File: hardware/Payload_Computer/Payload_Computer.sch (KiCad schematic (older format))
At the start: 0 parts

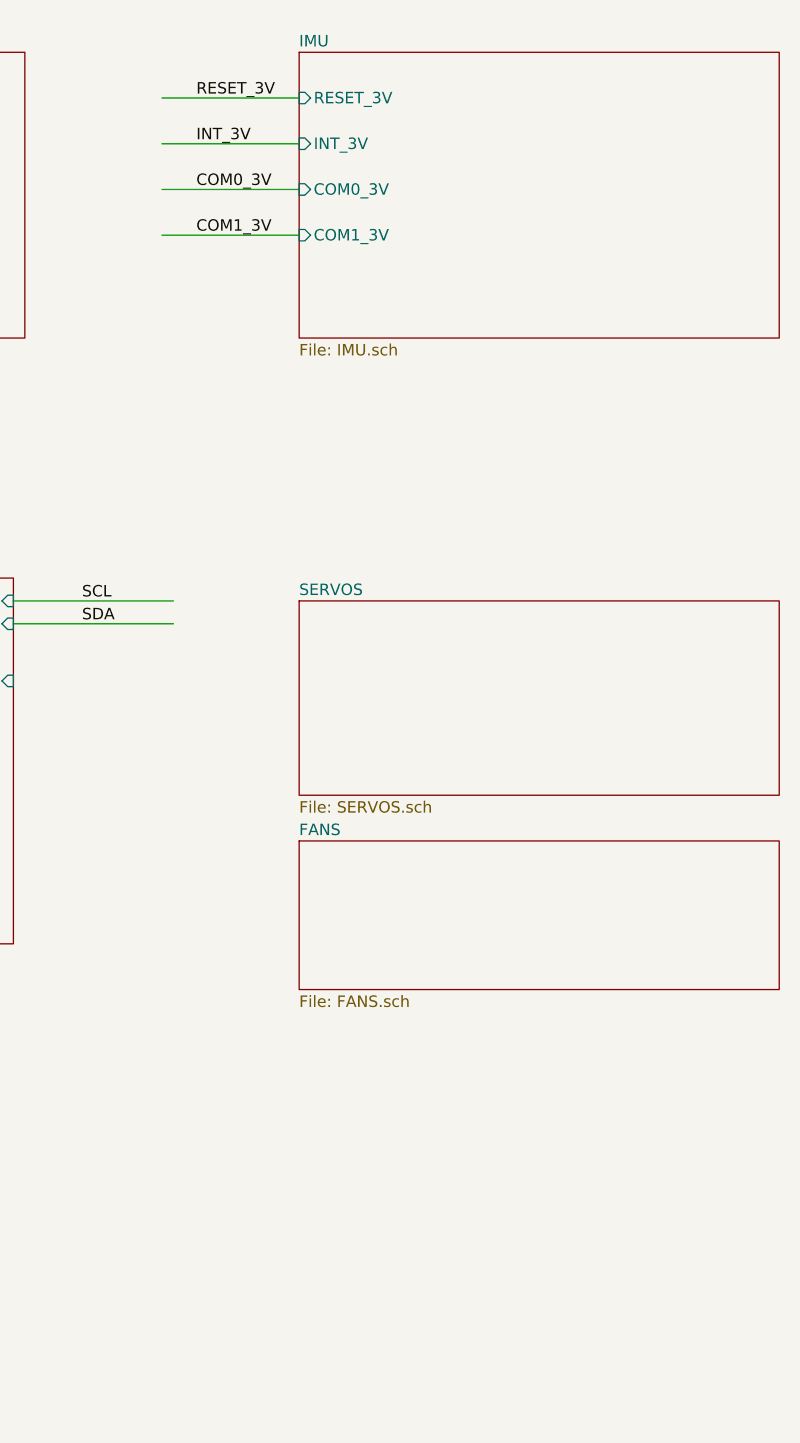
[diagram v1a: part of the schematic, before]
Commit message: Added Barometer, need to find Teensy SPI pin
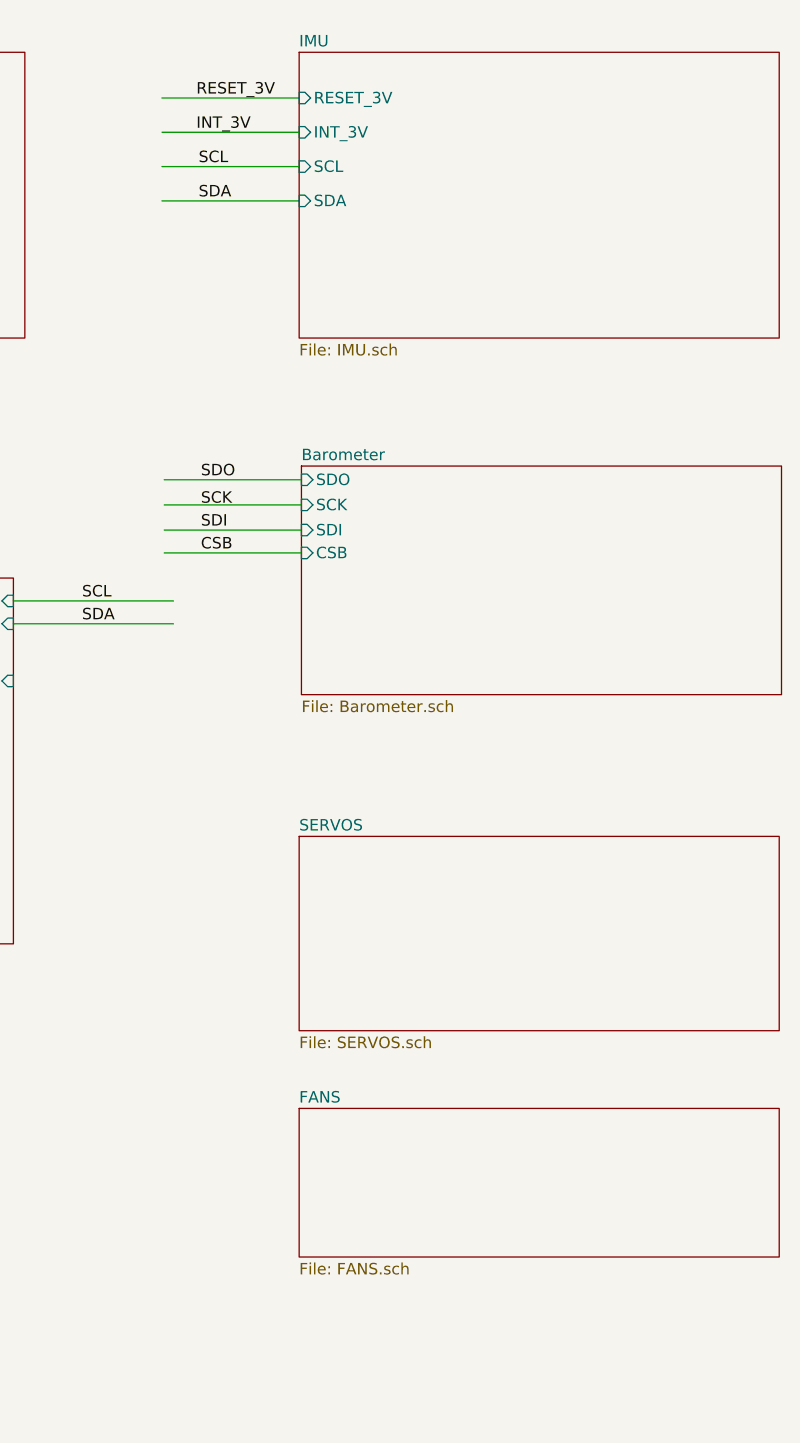
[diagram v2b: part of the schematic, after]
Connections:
- net labels added: CSB, SCK, SDI, SDO
- net labels removed: COM0_3V, COM1_3V
- wire segments 47 -> 51
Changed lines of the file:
@@
 $Descr A4 11693 8268
 encoding utf-8
-Sheet 1 24
+Sheet 1 27
 Title ""
 Date ""
@@
 F1 "IMU.sch" 50
 F2 "RESET_3V" I L 8100 900 50
-F3 "INT_3V" I L 8100 1100 50
-F4 "COM0_3V" I L 8100 1300 50
-F5 "COM1_3V" I L 8100 1500 50
+F3 "INT_3V" I L 8100 1050 50
+F4 "SCL" I L 8100 1200 50
+F5 "SDA" I L 8100 1350 50
 $EndSheet
 Wire Wire Line
 	8100 900  7500 900
 Wire Wire Line
-	8100 1100 7500 1100
-Wire Wire Line
-	8100 1300 7500 1300
-Wire Wire Line
-	8100 1500 7500 1500
+	8100 1050 7500 1050
+Wire Wire Line
+	8100 1200 7500 1200
+Wire Wire Line
+	8100 1350 7500 1350
 Text Label 7650 900  0    50   ~ 0
 RESET_3V
-Text Label 7650 1100 0    50   ~ 0
+Text Label 7650 1050 0    50   ~ 0
 INT_3V
-Text Label 7650 1300 0    50   ~ 0
-COM0_3V
-Text Label 7650 1500 0    50   ~ 0
-COM1_3V
+Text Label 7660 1200 0    50   ~ 0
+SCL
+Text Label 7660 1350 0    50   ~ 0
+SDA
 Wire Notes Line
 	2650 6100 2650 5300
@@
 $EndSheet
 $Sheet
-S 8100 3100 2100 850
+S 8100 4130 2100 850
 U 5FC5E24D
 F0 "SERVOS" 50
@@
 $EndSheet
 $Sheet
-S 8100 4150 2100 650
+S 8100 5320 2100 650
 U 5FC6109B
 F0 "FANS" 50
 F1 "FANS.sch" 50
 $EndSheet
+$Sheet
+S 8110 2510 2100 1000
+U 5FDA9108
+F0 "Barometer" 50
+F1 "Barometer.sch" 50
+F2 "SDO" I L 8110 2570 50
+F3 "SCK" I L 8110 2680 50
+F4 "SDI" I L 8110 2790 50
+F5 "CSB" I L 8110 2890 50
+$EndSheet
+Wire Wire Line
+	8110 2570 7510 2570
+Wire Wire Line
+	8110 2680 7510 2680
+Wire Wire Line
+	8110 2790 7510 2790
+Wire Wire Line
+	8110 2890 7510 2890
+Text Label 7670 2570 0    50   ~ 0
+SDO
+Text Label 7670 2690 0    50   ~ 0
+SCK
+Text Label 7670 2790 0    50   ~ 0
+SDI
+Text Label 7670 2890 0    50   ~ 0
+CSB
 $EndSCHEMATC

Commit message: Minor changes
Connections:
- net labels added: CS_BARO, CS_BARO2
- net labels removed: CSB, SCK, SDI, SDO
- wire segments 51 -> 52
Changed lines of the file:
@@
 $EndDescr
 $Sheet
-S 4750 700  2150 1250
+S 4100 700  2150 1250
 U 5F8457E8
 F0 "ARDUINO" 50
 F1 "ARDUINO.sch" 50
-F2 "XTAL1" I L 4750 800 50
-F3 "XTAL2" I L 4750 900 50
-F4 "TXD" I L 4750 1050 50
-F5 "RXD" I L 4750 1150 50
-F6 "RESET" I L 4750 1250 50
-F7 "MOSI" I L 4750 1400 50
-F8 "MISO" I L 4750 1500 50
-F9 "SCK" I L 4750 1600 50
+F2 "XTAL1" I L 4100 800 50
+F3 "XTAL2" I L 4100 900 50
+F4 "TXD" I L 4100 1050 50
+F5 "RXD" I L 4100 1150 50
+F6 "RESET" I L 4100 1250 50
+F7 "MOSI" I L 4100 1400 50
+F8 "MISO" I L 4100 1500 50
+F9 "SCK" I L 4100 1600 50
 $EndSheet
 $Sheet
@@
 	1850 1450 2600 1450
 Wire Wire Line
-	4750 800  3900 800
-Wire Wire Line
-	4750 900  3900 900
-Wire Wire Line
-	4750 3100 3900 3100
-Wire Wire Line
-	4750 3200 3900 3200
+	4100 800  3250 800
+Wire Wire Line
+	4100 900  3250 900
+Wire Wire Line
+	4100 3100 3250 3100
+Wire Wire Line
+	4100 3200 3250 3200
 Text Label 2050 800  0    50   ~ 0
 XTAL1_1
@@
 Text Label 2050 1450 0    50   ~ 0
 XTAL2_2
-Text Label 4150 800  0    50   ~ 0
+Text Label 3500 800  0    50   ~ 0
 XTAL1_1
-Text Label 4150 900  0    50   ~ 0
+Text Label 3500 900  0    50   ~ 0
 XTAL2_1
-Text Label 4150 3100 0    50   ~ 0
+Text Label 3500 3100 0    50   ~ 0
 XTAL1_2
-Text Label 4150 3200 0    50   ~ 0
+Text Label 3500 3200 0    50   ~ 0
 XTAL2_2
 Wire Notes Line
@@
 	1850 2400 2600 2400
 Wire Wire Line
-	4750 1050 3900 1050
-Wire Wire Line
-	4750 1150 3900 1150
-Wire Wire Line
-	4750 1250 3900 1250
-Text Label 4150 1250 0    50   ~ 0
+	4100 1050 3250 1050
+Wire Wire Line
+	4100 1150 3250 1150
+Wire Wire Line
+	4100 1250 3250 1250
+Text Label 3500 1250 0    50   ~ 0
 RESET_1
 Text Label 2050 2400 0    50   ~ 0
@@
 Text Label 2050 2300 0    50   ~ 0
 RXD_1
-Text Label 4150 1050 0    50   ~ 0
+Text Label 3500 1050 0    50   ~ 0
 RXD_1
-Text Label 4150 1150 0    50   ~ 0
+Text Label 3500 1150 0    50   ~ 0
 TXD_1
 Wire Notes Line
@@
 PROGRAMMING HEADERS\n
 Wire Wire Line
-	4750 3500 3900 3500
-Wire Wire Line
-	4750 3600 3900 3600
-Wire Wire Line
-	4750 3700 3900 3700
-Wire Wire Line
-	4750 1400 3900 1400
-Wire Wire Line
-	4750 1500 3900 1500
-Wire Wire Line
-	4750 1600 3900 1600
-Text Label 4150 1400 0    50   ~ 0
+	4100 3500 3250 3500
+Wire Wire Line
+	4100 3600 3250 3600
+Wire Wire Line
+	4100 3700 3250 3700
+Wire Wire Line
+	4100 1400 3250 1400
+Wire Wire Line
+	4100 1500 3250 1500
+Wire Wire Line
+	4100 1600 3250 1600
+Text Label 3500 1400 0    50   ~ 0
 MOSI_1
-Text Label 4150 1500 0    50   ~ 0
+Text Label 3500 1500 0    50   ~ 0
 MISO_1
-Text Label 4150 1600 0    50   ~ 0
+Text Label 3500 1600 0    50   ~ 0
 SCK_1
-Text Label 4150 3500 0    50   ~ 0
+Text Label 3500 3500 0    50   ~ 0
 MOSI_2
-Text Label 4150 3600 0    50   ~ 0
+Text Label 3500 3600 0    50   ~ 0
 MISO_2
-Text Label 4150 3700 0    50   ~ 0
+Text Label 3500 3700 0    50   ~ 0
 SCK_2
 $Sheet
@@
 RESET_TEENSY
 $Sheet
-S 4750 3000 2100 1600
+S 4100 3000 2100 1600
 U 5F84585C
 F0 "TEENSY 3.2" 50
 F1 "TEENSY 3.sch" 50
-F2 "XTAL1" I L 4750 3100 50
-F3 "XTAL2" I L 4750 3200 50
-F4 "RESET" I L 4750 3350 50
-F5 "MOSI" I L 4750 3500 50
-F6 "MISO" I L 4750 3600 50
-F7 "SCK" I L 4750 3700 50
-F8 "D+" I L 4750 3850 50
-F9 "D-" I L 4750 3950 50
-F10 "PTA0" I L 4750 4100 50
-F11 "PTA1" I L 4750 4200 50
-F12 "PTA2" I L 4750 4300 50
-F13 "PTA3" I L 4750 4400 50
-F14 "SCL" I R 6850 3100 50
-F15 "SDA" I R 6850 3200 50
-F16 "VBAT" I R 6850 3450 50
-$EndSheet
-Wire Wire Line
-	4750 3350 3900 3350
-Text Label 4050 3350 0    50   ~ 0
+F2 "XTAL1" I L 4100 3100 50
+F3 "XTAL2" I L 4100 3200 50
+F4 "RESET" I L 4100 3350 50
+F5 "MOSI" I L 4100 3500 50
+F6 "MISO" I L 4100 3600 50
+F7 "SCK" I L 4100 3700 50
+F8 "D+" I L 4100 3850 50
+F9 "D-" I L 4100 3950 50
+F10 "PTA0" I L 4100 4100 50
+F11 "PTA1" I L 4100 4200 50
+F12 "PTA2" I L 4100 4300 50
+F13 "PTA3" I L 4100 4400 50
+F14 "SCL" I R 6200 3100 50
+F15 "SDA" I R 6200 3200 50
+F16 "VBAT" I R 6200 3450 50
+$EndSheet
+Wire Wire Line
+	4100 3350 3250 3350
+Text Label 3400 3350 0    50   ~ 0
 RESET_TEENSY
 Wire Wire Line
-	4750 3850 3900 3850
-Wire Wire Line
-	4750 3950 3900 3950
-Wire Wire Line
-	4750 4100 3900 4100
-Text Label 4250 3850 0    50   ~ 0
+	4100 3850 3250 3850
+Wire Wire Line
+	4100 3950 3250 3950
+Wire Wire Line
+	4100 4100 3250 4100
+Text Label 3600 3850 0    50   ~ 0
 D+
-Text Label 4250 3950 0    50   ~ 0
+Text Label 3600 3950 0    50   ~ 0
 D-
 Wire Wire Line
-	4750 4200 3900 4200
-Wire Wire Line
-	4750 4300 3900 4300
-Wire Wire Line
-	4750 4400 3900 4400
-Text Label 4200 4100 0    50   ~ 0
+	4100 4200 3250 4200
+Wire Wire Line
+	4100 4300 3250 4300
+Wire Wire Line
+	4100 4400 3250 4400
+Text Label 3550 4100 0    50   ~ 0
 PTA0
-Text Label 4200 4200 0    50   ~ 0
+Text Label 3550 4200 0    50   ~ 0
 PTA1
-Text Label 4200 4300 0    50   ~ 0
+Text Label 3550 4300 0    50   ~ 0
 PTA2
-Text Label 4200 4400 0    50   ~ 0
+Text Label 3550 4400 0    50   ~ 0
 PTA3
 Wire Wire Line
-	6850 3100 7550 3100
-Wire Wire Line
-	6850 3200 7550 3200
-Text Label 7150 3100 0    50   ~ 0
+	6200 3100 6900 3100
+Wire Wire Line
+	6200 3200 6900 3200
+Text Label 6500 3100 0    50   ~ 0
 SCL
-Text Label 7150 3200 0    50   ~ 0
+Text Label 6500 3200 0    50   ~ 0
 SDA
 $Sheet
@@
 F1 "FANS.sch" 50
 $EndSheet
+Wire Wire Line
+	8110 2570 7510 2570
+Wire Wire Line
+	8110 2680 7510 2680
+Wire Wire Line
+	8110 2790 7510 2790
+Wire Wire Line
+	8110 2890 7510 2890
+Text Label 7670 2570 0    50   ~ 0
+MISO_2
+Text Label 7670 2690 0    50   ~ 0
+SCK_2
+Text Label 7670 2790 0    50   ~ 0
+MOSI_2
+Text Label 7670 2890 0    50   ~ 0
+CS_BARO
 $Sheet
 S 8110 2510 2100 1000
@@
 F0 "Barometer" 50
 F1 "Barometer.sch" 50
-F2 "SDO" I L 8110 2570 50
-F3 "SCK" I L 8110 2680 50
-F4 "SDI" I L 8110 2790 50
-F5 "CSB" I L 8110 2890 50
-$EndSheet
-Wire Wire Line
-	8110 2570 7510 2570
-Wire Wire Line
-	8110 2680 7510 2680
-Wire Wire Line
-	8110 2790 7510 2790
-Wire Wire Line
-	8110 2890 7510 2890
-Text Label 7670 2570 0    50   ~ 0
-SDO
-Text Label 7670 2690 0    50   ~ 0
-SCK
-Text Label 7670 2790 0    50   ~ 0
-SDI
-Text Label 7670 2890 0    50   ~ 0
-CSB
+F2 "SCK" I L 8110 2680 50
+F3 "CSB" I L 8110 2890 50
+F4 "MISO" I L 8110 2560 50
+F5 "MOSI" I L 8110 2790 50
+F6 "CS_BARO2" I L 8110 3000 50
+$EndSheet
+Wire Wire Line
+	8100 3000 7500 3000
+Text Label 7650 3000 0    50   ~ 0
+CS_BARO2
 $EndSCHEMATC

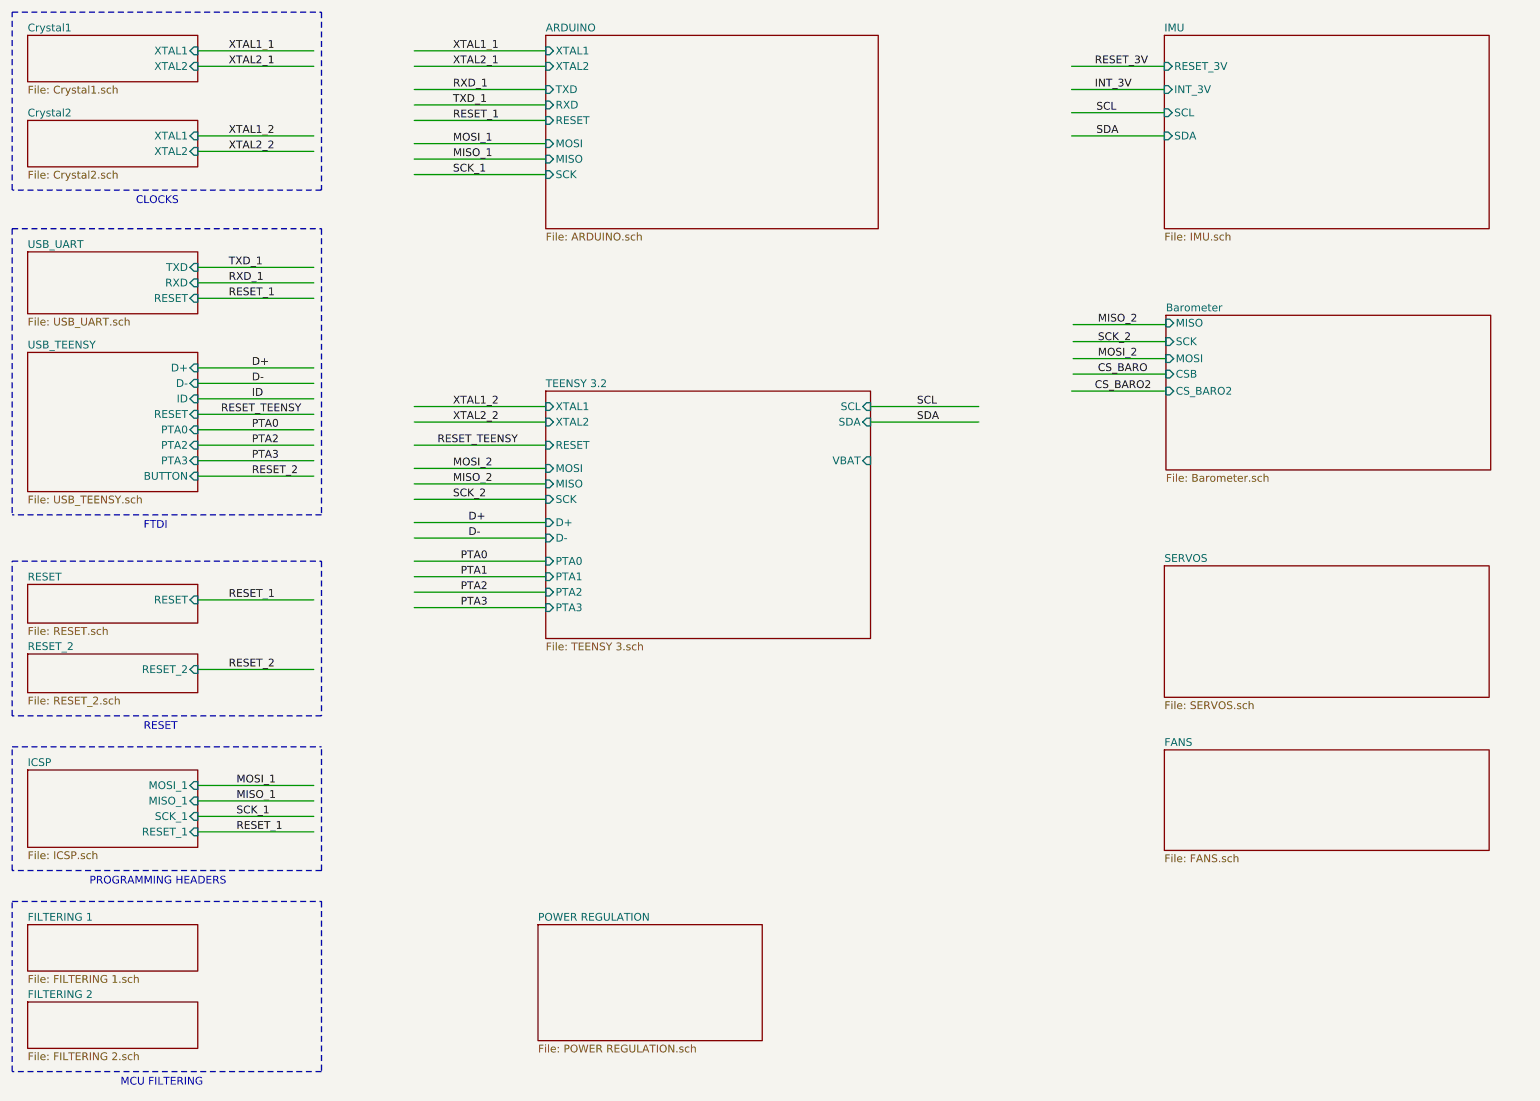
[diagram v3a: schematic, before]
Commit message: Updated processor for arduino. Fixed schematic a bit
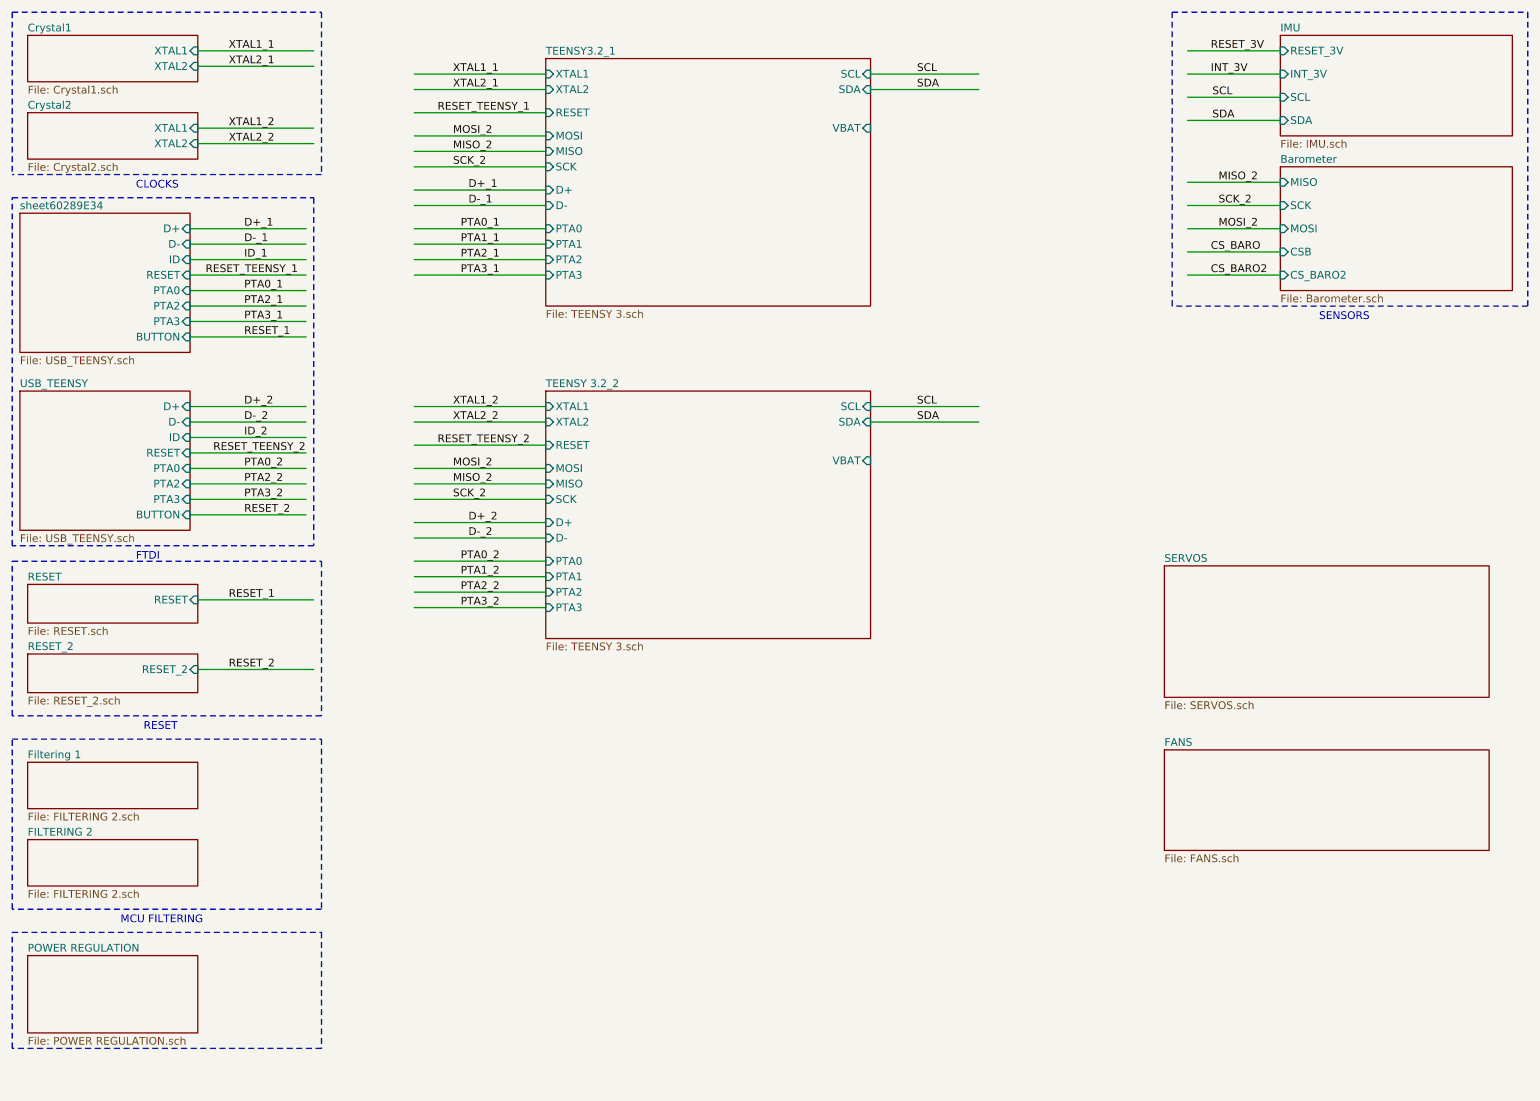
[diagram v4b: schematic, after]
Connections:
- net labels added: D+_1, D+_2, D-_1, D-_2, ID_1, ID_2, PTA0_1, PTA0_2, PTA1_1, PTA1_2, PTA2_1, PTA2_2, PTA3_1, PTA3_2, RESET_TEENSY_1, RESET_TEENSY_2
- net labels removed: D+, D-, ID, MISO_1, MOSI_1, PTA0, PTA1, PTA2, PTA3, RESET_TEENSY, RXD_1, SCK_1, TXD_1
- wire segments 52 -> 59
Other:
- note added: "SENSORS\n"
- note removed: "PROGRAMMING HEADERS\n"

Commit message: Finished Fan Schematic. Working on Servos
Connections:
- net labels removed: ID_1, ID_2
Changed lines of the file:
@@
 $Descr A4 11693 8268
 encoding utf-8
-Sheet 1 26
+Sheet 1 22
 Title ""
 Date ""
@@
 D-_2
 Text Label 2150 3300 0    50   ~ 0
-ID_2
+PTA1_2
 Text Label 2150 3500 0    50   ~ 0
 PTA0_2
@@
 F14 "SCL" I R 6200 3100 50
 F15 "SDA" I R 6200 3200 50
-F16 "VBAT" I R 6200 3450 50
 $EndSheet
 Wire Wire Line
@@
 $EndSheet
 $Sheet
-S 8100 5320 2100 650
+S 8100 5320 2100 280
 U 5FC6109B
 F0 "FANS" 50
 F1 "FANS.sch" 50
+F2 "FAN_CONTROL" I L 8100 5450 50
 $EndSheet
 Wire Wire Line
@@
 F14 "SCL" I R 6200 950 50
 F15 "SDA" I R 6200 1050 50
-F16 "VBAT" I R 6200 1300 50
 $EndSheet
 Wire Wire Line
@@
 D-_1
 Text Label 2150 2150 0    50   ~ 0
-ID_1
+PTA1_1
 Text Label 2150 2350 0    50   ~ 0
 PTA0_1

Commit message: Minor Changes
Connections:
- net labels added: FANS, MISO, MOSI, SCK, SERVO1, SERVO2, SERVO3, SERVO4
- wire segments 59 -> 64
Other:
- note added: "SERVOS\n"

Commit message: Added LED to board
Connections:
- net labels added: LED_BLUE, LED_GREEN, LED_RED
- wire segments 64 -> 67
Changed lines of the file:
@@
 $Descr A4 11693 8268
 encoding utf-8
-Sheet 1 18
+Sheet 1 19
 Title ""
 Date ""
@@
 F14 "PWM4" I R 6200 1250 50
 $EndSheet
+$Sheet
+S 8850 4500 1450 450
+U 60334804
+F0 "LED" 50
+F1 "LED.sch" 50
+F2 "LED_RED" I L 8850 4600 50
+F3 "LED_GREEN" I L 8850 4700 50
+F4 "LED_BLUE" I L 8850 4800 50
+$EndSheet
+Wire Wire Line
+	8850 4600 8250 4600
+Wire Wire Line
+	8850 4700 8250 4700
+Wire Wire Line
+	8850 4800 8250 4800
+Text Label 8400 4600 0    50   ~ 0
+LED_RED
+Text Label 8400 4700 0    50   ~ 0
+LED_GREEN
+Text Label 8400 4800 0    50   ~ 0
+LED_BLUE
 $EndSCHEMATC

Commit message: Minor Changes
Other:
- note added: "FANS\n"
- note added: "LED\n"
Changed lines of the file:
@@
 $EndSheet
 $Sheet
-S 8850 4500 1450 450
+S 8850 4500 1500 400
 U 60334804
 F0 "LED" 50
@@
 Text Label 8400 4800 0    50   ~ 0
 LED_BLUE
+Wire Notes Line
+	8150 5000 10450 5000
+Wire Notes Line
+	10450 5000 10450 4400
+Wire Notes Line
+	10450 4400 8150 4400
+Wire Notes Line
+	8150 4400 8150 5000
+Text Notes 9150 5100 0    50   ~ 0
+LED\n
+Text Notes 9200 4300 0    50   ~ 0
+FANS\n
 $EndSCHEMATC
